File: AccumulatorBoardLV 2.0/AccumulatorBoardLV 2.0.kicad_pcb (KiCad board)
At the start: 4 copper layers, 152.4 x 50.8 mm, 66 parts, among them J1 Contactor 1, J10 To HV Board, J11 IMD Reset, J12 TS Interlock, J13 Temp Reset, J14 To ECU, J15 Charger LV, J16 Charger Interlock, J17 Lid Interlock, J18 From HV Board, J19 Chip 1, J2 Contactor 2, J20 Chip 2, J21 Chip 3, J22 Chip 4, J3 IMD LV, J4 BMS Connector 1, J5 BMS Connector 2, J6 BMS TX, J7 BMS RX, J8 Current Sensor, J9 BMS Reset, U1 DE1A1B-L2-12V, U10 MCP3008, U11 ISO1050, U12 stm_nucleo_FK303K8, U13 MCP3008, U14 MCP3008, U2 LM555N, U3 SN754410, U4 DE1A1B-L2-12V, U5 L78S05CV-DG, U6 DE1A1B-L2-12V, U7 DK1A1B-12V, U8 ADUM4154ARIZ, U9 MCP3008

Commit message: final lv board routed
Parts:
- removed C11, C12, C13: 1uF, Capacitors_SMD:C_0805_HandSoldering
- removed D1, D2: D, Diodes_SMD:D_1206
- removed H1, H2: MtngHole, Mounting_Holes:MountingHole_4.5mm
- removed J13: Temp Reset, Connectors_Molex:Molex_NanoFit_1x02x2.50mm_Straight
- removed J18: From HV Board, Connectors_Molex:Molex_NanoFit_1x02x2.50mm_Straight
- removed J19: Chip 1, Connectors_Molex:Molex_NanoFit_2x05x2.50mm_Straight
- removed J20: Chip 2, Connectors_Molex:Molex_NanoFit_2x05x2.50mm_Straight
- removed J21: Chip 3, Connectors_Molex:Molex_NanoFit_2x05x2.50mm_Straight
- removed J22: Chip 4, Connectors_Molex:Molex_NanoFit_2x05x2.50mm_Straight
- removed J5: BMS Connector 2, Connectors_Molex:Molex_NanoFit_2x06x2.50mm_Straight
- removed J6: BMS TX, Connectors_Molex:Molex_NanoFit_1x02x2.50mm_Straight
- removed J7: BMS RX, Connectors_Molex:Molex_NanoFit_1x02x2.50mm_Straight
- removed U10, U13, U14, U9: MCP3008, Housings_SOIC:SOIC-16_3.9x9.9mm_Pitch1.27mm
- removed U8: ADUM4154ARIZ, Housings_SOIC:SOIC-20W_7.5x12.8mm_Pitch1.27mm
- added L1: HM2113ZNL, FSFootprints:HM2113ZNL, F.Cu at (159.7, 145.8)
- added R10: 680, Resistors_SMD:R_0805_HandSoldering, F.Cu at (140.0, 122.9)
- added R11: 402, Resistors_SMD:R_0805_HandSoldering, F.Cu at (145.1, 122.9)
- added R12: 22, Resistors_SMD:R_0805_HandSoldering, F.Cu at (169.8, 142.0)
- added R13: 22, Resistors_SMD:R_0805_HandSoldering, F.Cu at (169.8, 147.0)
- added R9: 1.5k, Resistors_SMD:R_0805_HandSoldering, F.Cu at (140.0, 120.4)
- C1, C4, C5: footprint Capacitors_THT:CP_Radial_D5.0mm_P2.50mm -> Capacitors_SMD:C_0805_HandSoldering
- C10: value 1uF -> 10nF; moved to F.Cu
- C2, C3, C6, C8: footprint Capacitors_THT:C_Disc_D3.0mm_W1.6mm_P2.50mm -> Capacitors_SMD:C_0805_HandSoldering
- C7: value 0.1uF -> 15pF; footprint Capacitors_THT:C_Disc_D3.0mm_W1.6mm_P2.50mm -> Capacitors_SMD:C_0805_HandSoldering
- C9: footprint Capacitors_THT:C_Disc_D4.3mm_W1.9mm_P5.00mm -> Capacitors_SMD:C_0805_HandSoldering
- J14: value To ECU -> To ECU in PE Box
- J4: value BMS Connector 1 -> Conn_01x02_Male; footprint Connectors_Molex:Molex_NanoFit_2x03x2.50mm_Straight -> Connectors_Molex:Molex_NanoFit_1x02x2.50mm_Straight
- R1, R2: value 1.1kR -> 1.1k
- R4, R8: value R -> 1.1k
- R5, R7: value R -> 2.2k
- U1: value DE1A1B-L2-12V -> LTC6820; footprint FSFootprints:DE1A1B-L2-12V -> FSFootprints:MSOP-16_[LTC6820]_10_thou_compat
- moved U1 96.6 mm to (140.6, 127.4)
- moved J4 53.6 mm to (170.4, 136.9)
- moved J9 51.3 mm to (46.1, 110.2), turned to 270 degrees
- moved J16 46.3 mm to (99.3, 114.1), turned to 180 degrees
- moved R4 42.5 mm to (126.0, 122.3), turned to 90 degrees
- moved R5 39.6 mm to (128.5, 122.3), turned to 270 degrees
- moved J11 36.7 mm to (46.1, 117.9), turned to 270 degrees
- moved J17 36.2 mm to (106.9, 114.1), turned to 180 degrees
- moved J8 35.7 mm to (117.1, 119.7), turned to 0 degrees
- moved C10 35.6 mm to (152.7, 138.2), turned to 90 degrees
- moved J12 32.3 mm to (108.2, 119.7), turned to 0 degrees
- moved J10 31.4 mm to (129.8, 114.1), turned to 180 degrees
- moved C5 27.1 mm to (108.2, 126.7), turned to 0 degrees
- moved C4 26.6 mm to (114.6, 126.7), turned to 180 degrees
- moved C6 24.9 mm to (131.1, 142.0), turned to 90 degrees
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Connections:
- net /12V_SRC renamed 12V_SRC
- net /AIRS_ACC_OUT renamed AIRS_ACC_OUT
- net /AIRS_FINAL renamed AIRS_FINAL
- net /AIRS_FINAL_CHARGER renamed AIRS_FINAL_CHARGER
- net /AIRS_LID_OUT renamed AIRS_LID_OUT
- net /BMS_FLT_LATCHED renamed BMS_FLT_LAT
- net /BMS_RESET renamed BMS_RESET
- net /CAN_H renamed CAN_H
- net /CAN_L renamed CAN_L
- net /CAN_RX renamed CAN_RX
- net /CAN_TX renamed CAN_TX
- net /IMD_FLT renamed IMD_FLT
- net /IMD_FLT_H renamed IMD_FLT_H
- net /IMD_FLT_LATCHED renamed IMD_FLT_LAT
- net /IMD_RESET renamed IMD_RESET
- net /TEMP_FLT renamed BMS_FLT
- net /TIMER renamed TIMER
- C10 pad 1: /3.3V_TS -> Net-(C10-Pad1)
- C10 pad 2: /BATT- -> GND
- C7 pad 1: /3.3V_TS -> Net-(C7-Pad1)
- C7 pad 2: /BATT- -> Net-(C7-Pad2)
- D3 pad 1: /TIMER_H -> TIMER_H
- D3 pad 2: /BMS_FLT -> BMS_FLT_H
- D4 pad 1: /TIMER_H -> TIMER_H
- D5 pad 1: /TIMER_H -> TIMER_H
- D6 pad 1: /TIMER_H -> TIMER_H
- D7 pad 1: /TIMER_H -> TIMER_H
- J14 pad 11: /5V_BMS -> +5V
- J14 pad 12: /SIG_CURRENT -> SIG_CURRENT
- J14 pad 4: /V_L -> (no net)
- J14 pad 7: /AIRS_CHARGER_OUT -> AIRS_CHARGER_OUT
- J15 pad 3: /V_S -> (no net)
- J15 pad 4: /AIRS_CHARGER_OUT -> AIRS_CHARGER_OUT
- J15 pad 6: /CHARGER_CONTROL -> CHARGER_CONTROL_H
- J17 pad 1: (no net) -> /AIRS_RELAYS_OUT
- J3 pad 6: (no net) -> Net-(J3-Pad6)
- J4 pad 1: /BMS_FLT -> Net-(J4-Pad1)
- J4 pad 2: /V_L -> Net-(J4-Pad2)
- J8 pad 1: /5V_BMS -> +5V
- J8 pad 2: /SIG_CURRENT -> Net-(J8-Pad2)
- R1 pad 1: /IMD_FLT_5 -> Net-(R1-Pad1)
- R2 pad 1: /IMD_FLT_5 -> GND
- R2 pad 2: GND -> Net-(R1-Pad1)
- R4 pad 1: /3.3V_TS -> SIG_CURRENT
- R4 pad 2: /TEMP_SS_0 -> Net-(J8-Pad2)
- R5 pad 1: /3.3V_TS -> GND
- R5 pad 2: /TEMP_SS_1 -> SIG_CURRENT
- R7 pad 1: /3.3V_TS -> IMD_STATUS
- R7 pad 2: /TEMP_SS_2 -> Net-(J3-Pad6)
- R8 pad 1: /3.3V_TS -> GND
- R8 pad 2: /TEMP_SS_3 -> IMD_STATUS
- U1 pad 1: /TIMER_H -> +3V3
- U1 pad 2: /TIMER_H -> Net-(U1-Pad2)
- U1 pad 3: /TEMP_FLT_LATCHED -> Net-(U1-Pad3)
- U1 pad 4: GND -> Net-(U1-Pad4)
- U1 pad 5: /AIRS_CHARGER_OUT -> Net-(U1-Pad5)
- U1 pad 6: /AIRS_TEMP_OUT -> +3V3
- U1 pad 7: /TEMP_RESET -> GND
- U1 pad 8: /TEMP_FLT_H -> GND
- U12 pad 10: /TEMP_FLT_LATCHED -> IMD_STATUS
- U12 pad 19: (no net) -> SIG_CURRENT
- U12 pad 20: Net-(U12-Pad20) -> (no net)
- U12 pad 21: Net-(U12-Pad21) -> (no net)
- U12 pad 22: Net-(U12-Pad22) -> Net-(U1-Pad5)
- U12 pad 23: Net-(U12-Pad23) -> Net-(U1-Pad4)
- U12 pad 24: Net-(U12-Pad24) -> Net-(U1-Pad3)
- U12 pad 25: Net-(U12-Pad25) -> Net-(U1-Pad2)
- U12 pad 9: (no net) -> CHARGER_CONTROL
- U3 pad 10: (no net) -> CHARGER_CONTROL
- U3 pad 11: (no net) -> CHARGER_CONTROL_H
- U3 pad 14: /TIMER_H -> TIMER_H
- U3 pad 3: /TEMP_FLT_H -> BMS_FLT_H
- U3 pad 7: /IMD_FLT_5 -> Net-(R1-Pad1)
- U4 pad 1: /TIMER_H -> TIMER_H
- U4 pad 2: /TIMER_H -> TIMER_H
- U4 pad 5: /AIRS_TEMP_OUT -> AIRS_CHARGER_OUT
- U4 pad 8: /BMS_FLT -> BMS_FLT_H
- U6 pad 1: /TIMER_H -> TIMER_H
- U6 pad 2: /TIMER_H -> TIMER_H
- U7 pad 4: (no net) -> /AIRS_RELAYS_OUT
- U7 pad 8: /TIMER_H -> TIMER_H
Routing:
- net GND: track 23.3 -> 384.5 mm, vias 2 -> 0
- net /5V_BMS: track 175.3 -> 0.00 mm
- net +5V: track 4.23 -> 151.5 mm, vias 0 -> 1
- net /SIG_CURRENT: track 134.0 -> 0.00 mm
- net TIMER_H: track 0.00 -> 126.8 mm, vias 0 -> 1
- net SIG_CURRENT: track 0.00 -> 125.7 mm, vias 0 -> 1
- net /TEMP_FLT_LATCHED: track 110.3 -> 0.00 mm
- net /TIMER_H: track 105.1 -> 0.00 mm, vias 1 -> 0
- net BMS_FLT_H: track 0.00 -> 104.4 mm
- net /V_L: track 89.6 -> 0.00 mm
- net /AIRS_CHARGER_OUT: track 87.3 -> 0.00 mm
- net /BATT-: track 77.0 -> 0.00 mm, vias 5 -> 0
- net CHARGER_CONTROL: track 0.00 -> 73.9 mm
- net /SCLK: track 67.5 -> 0.00 mm, vias 3 -> 0
- net /TEMP_FLT_H: track 66.1 -> 0.00 mm, vias 1 -> 0
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- removed copper zone on In1.Cu, net +5V
- removed copper zone on In1.Cu, net /3.3V_TS
- removed copper zone on In2.Cu, net /BATT-
- removed copper zone on In2.Cu, net GND
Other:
- board size 152.4 x 50.8 mm -> 133.4 x 44.9 mm
- copper layers 4 -> 2
- net class HighSpeed: via_dia 100 -> 100.000003; via_drill 50 -> 50.000002
- net class Power: via_dia 100 -> 100.000003

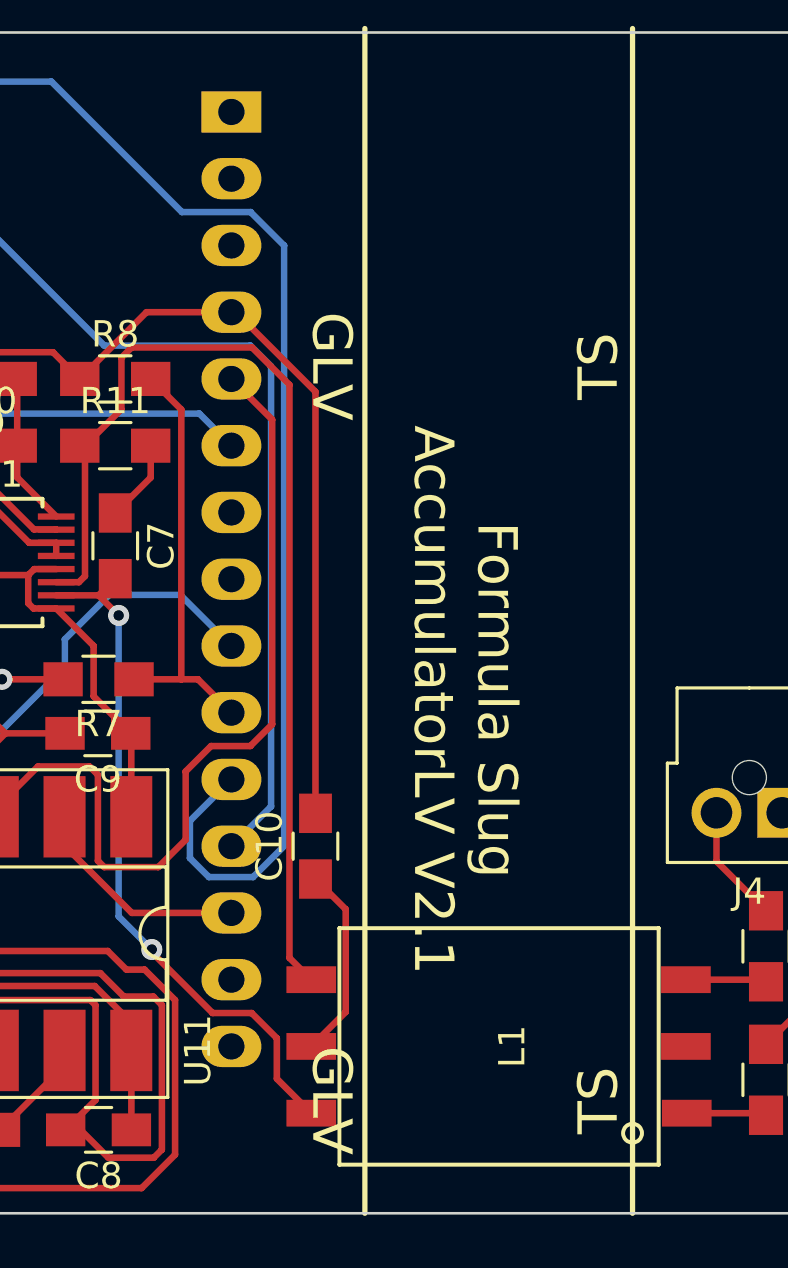
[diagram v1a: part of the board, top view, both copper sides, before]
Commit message: Add termination resistor to isoSPI on Accumulator LV
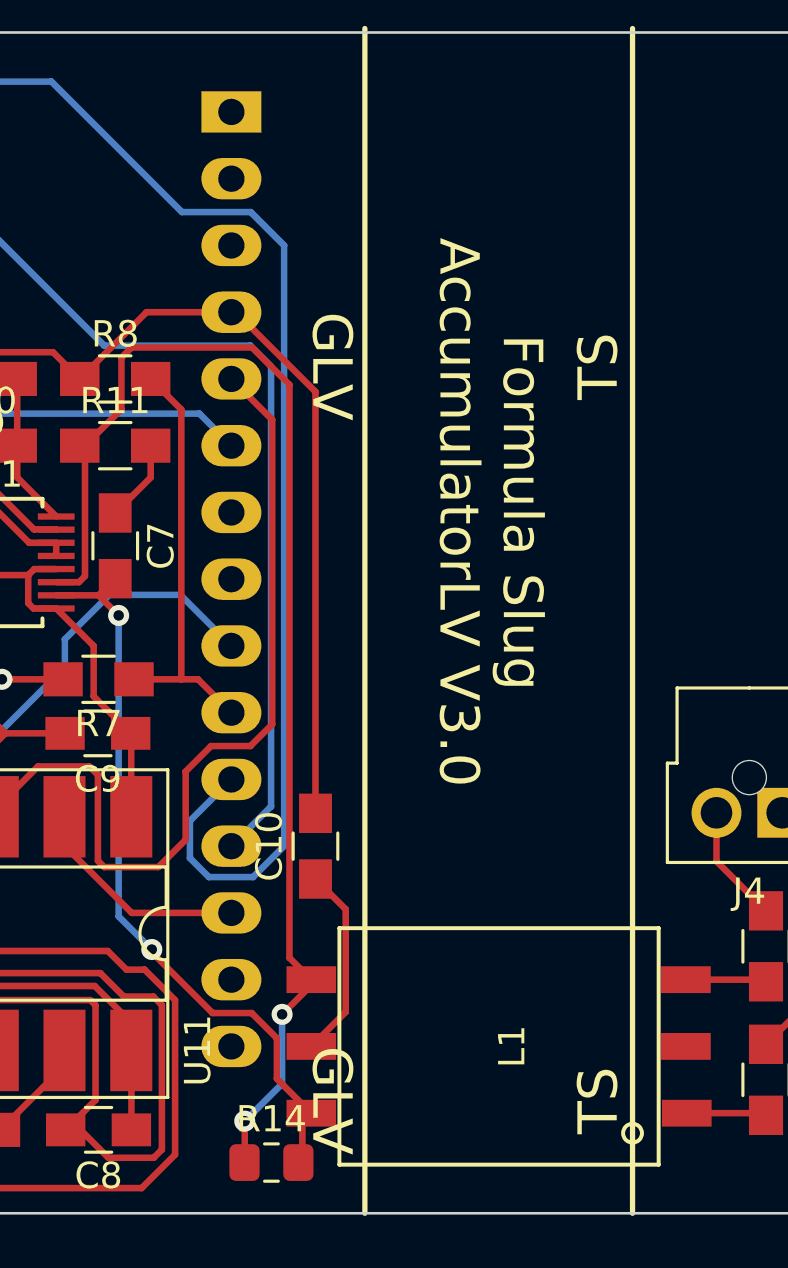
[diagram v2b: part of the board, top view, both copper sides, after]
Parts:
- added R14: 200, Resistor_SMD:R_0805_2012Metric_Pad1.15x1.40mm_HandSolder, F.Cu at (151.0, 150.2)
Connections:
- J14 pad 13: (no net) -> Net-(J14-Pad13)
- J14 pad 14: (no net) -> Net-(J14-Pad14)
- J14 pad 4: (no net) -> Net-(J14-Pad4)
- J14 pad 9: (no net) -> Net-(J14-Pad9)
- J15 pad 3: (no net) -> Net-(J15-Pad3)
- J15 pad 7: (no net) -> Net-(J15-Pad7)
- L1 pad 2: (no net) -> Net-(L1-Pad2)
- U12 pad 1: (no net) -> Net-(U12-Pad1)
- U12 pad 14: (no net) -> Net-(U12-Pad14)
- U12 pad 15: (no net) -> Net-(U12-Pad15)
- U12 pad 16: (no net) -> Net-(U12-Pad16)
- U12 pad 18: (no net) -> Net-(U12-Pad18)
- U12 pad 2: (no net) -> Net-(U12-Pad2)
- U12 pad 20: (no net) -> Net-(U12-Pad20)
- U12 pad 21: (no net) -> Net-(U12-Pad21)
- U12 pad 26: (no net) -> Net-(U12-Pad26)
- U12 pad 27: (no net) -> Net-(U12-Pad27)
- U12 pad 28: (no net) -> Net-(U12-Pad28)
- U12 pad 3: (no net) -> Net-(U12-Pad3)
- U12 pad 7: (no net) -> Net-(U12-Pad7)
- U12 pad 8: (no net) -> Net-(U12-Pad8)
- U2 pad 5: (no net) -> Net-(U2-Pad5)
- U2 pad 7: (no net) -> Net-(U2-Pad7)
- U7 pad 5: (no net) -> Net-(U7-Pad5)
- U7 pad 6: (no net) -> Net-(U7-Pad6)
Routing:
- net Net-(L1-Pad4): track 40.4 -> 48.5 mm, vias 0 -> 2
- net Net-(C7-Pad2): track 26.4 -> 28.5 mm
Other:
- board text added: "Formula Slug AccumulatorLV V3.0"
- board text removed: "Formula Slug AccumulatorLV V2.1"
